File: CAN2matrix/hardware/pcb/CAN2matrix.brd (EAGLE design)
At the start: 100 x 80 mm, 33 parts, among them IC1 MEGA8-P, IC2 MCP2515-E/P, IC3 MCP2515-E/P, U1 MCP2551P, U2 MCP2551P, X1 CAN1, X2 CAN2

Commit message: V1.0 of PCB and adjusted schematics
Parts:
- R4, R5, R6, R7, R8: device resistor:0207/2V -> resistor:0207/10
- R9: device resistor:0207/2V -> resistor:0204/7
- moved R1 53.9 mm to (78.7, 39.4)
- moved PH1 44.4 mm to (29.2, 33.0), turned to 0 degrees
- moved R9 43.1 mm to (30.5, 27.9), turned to 180 degrees
- moved R8 23.2 mm to (44.5, 67.3)
- moved LED5 22.9 mm to (44.5, 76.2)
- moved R4 18.2 mm to (64.8, 67.3)
- moved LED1 17.8 mm to (64.8, 76.2)
- moved R7 13.3 mm to (49.5, 67.3)
- moved LED4 12.7 mm to (49.5, 76.2)
- moved C8 10.2 mm to (40.6, 41.9), turned to 180 degrees
- moved R5 8.52 mm to (59.7, 67.3)
- moved LED2 7.62 mm to (59.7, 76.2)
- moved R6 4.58 mm to (54.6, 67.3)
- moved LED3 2.54 mm to (54.6, 76.2)
- moved C4 1.27 mm to (69.8, 26.7)
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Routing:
- net GND: track 0.00 -> 371.3 mm
- net +5V: track 0.00 -> 213.0 mm
- net N$9: track 0.00 -> 148.2 mm
- net N$1: track 0.00 -> 121.4 mm
- net N$2: track 0.00 -> 116.1 mm
- net N$3: track 0.00 -> 101.3 mm
- net N$16: track 0.00 -> 55.8 mm
- net N$22: track 0.00 -> 50.1 mm
- net N$14: track 0.00 -> 49.7 mm
- net N$7: track 0.00 -> 46.6 mm
- net N$23: track 0.00 -> 43.3 mm
- net N$17: track 0.00 -> 40.9 mm
- net N$19: track 0.00 -> 40.2 mm
- net N$15: track 0.00 -> 36.6 mm
- net N$24: track 0.00 -> 36.4 mm
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- added copper zone on layer 1, net +5V
- added copper zone on layer 16, net GND
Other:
- outline, holes or cut-outs redrawn
- board text added: "Dual CAN"
- board text added: "V1.0"
- board text added: "dev@layer128.net"

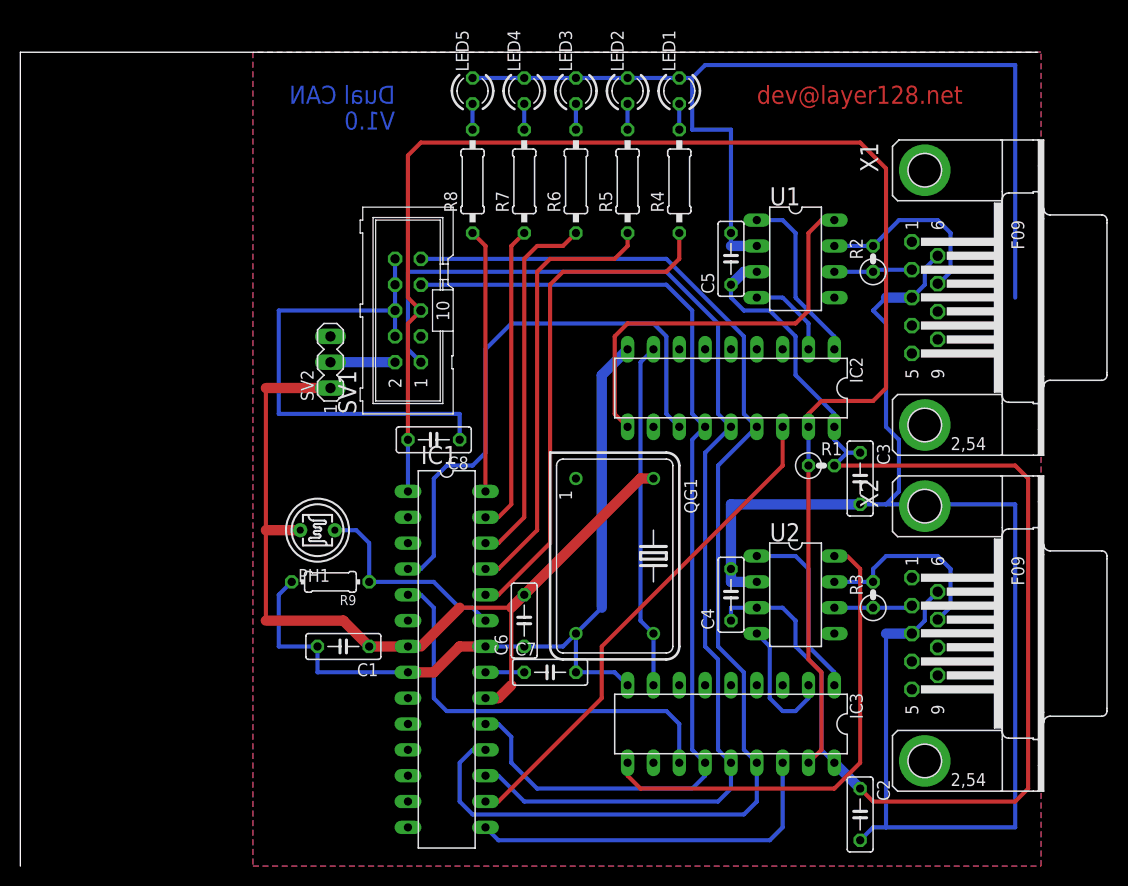
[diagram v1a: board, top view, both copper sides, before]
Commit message: add non-USB power supply to schematics and PCB; export images
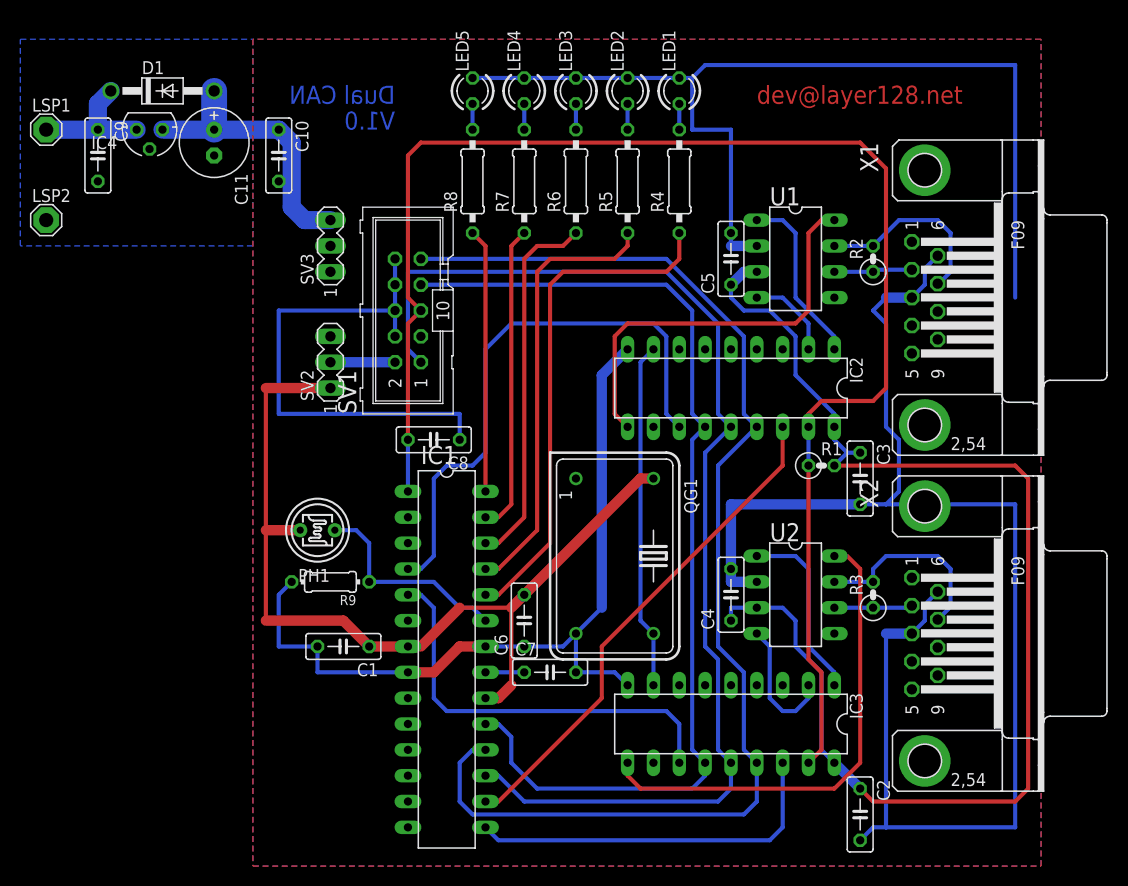
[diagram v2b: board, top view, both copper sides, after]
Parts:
- added C10: 100n, resistor:C050-025X075
- added C11: 1µ, resistor:E2,5-7
- added C9: 330n, resistor:C050-025X075
- added D1: 1N4002, diode:DO41-10
- added IC4: (no value), v-reg:78LXX
- added LSP1: +12V, solpad:SE14
- added LSP2: SE14, solpad:SE14
- added SV3: Ext Pwr, con-lstb:MA03-1
- SV2: value Ext Pwr -> USB Pwr
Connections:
- new net +12V: C9.1, D1.C, IC4.IN, LSP1.MP
- new net N$33: C10.1, C11.+, D1.A, IC4.OUT, SV3.3
- net +5V: now also SV3.2
- net GND: now also C10.2, C11.-, C9.2, IC4.GND, LSP2.MP
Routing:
- net N$33: track 0.00 -> 27.7 mm
- net +12V: track 0.00 -> 13.2 mm
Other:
- board outline removed
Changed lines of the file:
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@@
 <board>
 <plain>
-<wire x1="100" y1="80" x2="0" y2="80" width="0" layer="20"/>
-<wire x1="0" y1="80" x2="0" y2="0" width="0" layer="20"/>
 <text x="36.83" y="74.93" size="1.778" layer="16" rot="MR0">Dual CAN</text>
 <text x="36.83" y="72.39" size="1.778" layer="16" rot="MR0">V1.0</text>
@@
 <attribute name="OC_FARNELL" value="unknown" x="81.28" y="-38.1" size="1.778" layer="27" rot="R270" display="off"/>
 </element>
-<element name="SV2" library="con-lstb" package="MA03-1" value="Ext Pwr" x="30.48" y="49.53" rot="R90">
+<element name="SV2" library="con-lstb" package="MA03-1" value="USB Pwr" x="30.48" y="49.53" rot="R90">
 <attribute name="OC_NEWARK" value="unknown" x="90.17" y="128.27" size="1.778" layer="27" rot="R90" display="off"/>
 <attribute name="MPN" value="" x="90.17" y="128.27" size="1.778" layer="27" rot="R90" display="off"/>
@@
 <element name="R9" library="resistor" package="0204/7" value="39k" x="30.48" y="27.94" rot="R180"/>
 <element name="PH1" library="photo-elements" package="T0-46-A10XX" value="A1050_09" x="29.21" y="33.02"/>
+<element name="IC4" library="v-reg" package="78LXX" value="" x="12.7" y="72.39" rot="R180"/>
+<element name="C9" library="resistor" package="C050-025X075" value="330n" x="7.62" y="69.85" rot="R270"/>
+<element name="C10" library="resistor" package="C050-025X075" value="100n" x="25.4" y="69.85" rot="R270"/>
+<element name="C11" library="resistor" package="E2,5-7" value="1µ" x="19.05" y="71.12" rot="R270"/>
+<element name="D1" library="diode" package="DO41-10" value="1N4002" x="13.97" y="76.2"/>
+<element name="SV3" library="con-lstb" package="MA03-1" value="Ext Pwr" x="30.48" y="60.96" rot="R90">
+<attribute name="OC_NEWARK" value="unknown" x="30.48" y="60.96" size="1.778" layer="27" rot="R90" display="off"/>
+<attribute name="MPN" value="" x="30.48" y="60.96" size="1.778" layer="27" rot="R90" display="off"/>
+<attribute name="MF" value="" x="30.48" y="60.96" size="1.778" layer="27" rot="R90" display="off"/>
+<attribute name="OC_FARNELL" value="unknown" x="30.48" y="60.96" size="1.778" layer="27" rot="R90" display="off"/>
+</element>
+<element name="LSP1" library="solpad" package="SE14" value="+12V" x="2.54" y="72.39"/>
+<element name="LSP2" library="solpad" package="SE14" value="SE14" x="2.54" y="63.5"/>
 </elements>
 <signals>
@@
 <wire x1="71.12" y1="58.42" x2="72.39" y2="58.42" width="1.016" layer="16"/>
 <polygon width="0.4064" layer="1" orphans="yes">
-<vertex x="22.86" y="80.01"/>
+<vertex x="22.86" y="81.28"/>
 <vertex x="22.86" y="0"/>
 <vertex x="100.33" y="0"/>
-<vertex x="100.33" y="80.01"/>
+<vertex x="100.33" y="81.28"/>
 </polygon>
+<contactref element="SV3" pad="2"/>
 </signal>
 <signal name="GND">
@@
 <wire x1="43.18" y1="44.45" x2="25.4" y2="44.45" width="0.4064" layer="16"/>
 <polygon width="0.4064" layer="16" orphans="yes">
-<vertex x="22.86" y="80.01"/>
+<vertex x="22.86" y="81.28"/>
 <vertex x="22.86" y="0"/>
 <vertex x="100.33" y="0"/>
-<vertex x="100.33" y="80.01"/>
+<vertex x="100.33" y="81.28"/>
+</polygon>
+<contactref element="C9" pad="2"/>
+<contactref element="IC4" pad="GND"/>
+<contactref element="C11" pad="-"/>
+<contactref element="C10" pad="2"/>
+<contactref element="LSP2" pad="MP"/>
+<polygon width="0.4064" layer="16" orphans="yes">
+<vertex x="0" y="60.96"/>
+<vertex x="0" y="81.28"/>
+<vertex x="22.86" y="81.28"/>
+<vertex x="22.86" y="60.96"/>
 </polygon>
 </signal>
@@
 <wire x1="30.48" y1="33.02" x2="30.91" y2="33.02" width="0" layer="19" extent="16-16"/>
 </signal>
+<signal name="+12V">
+<contactref element="D1" pad="C"/>
+<contactref element="IC4" pad="IN"/>
+<contactref element="C9" pad="1"/>
+<contactref element="LSP1" pad="MP"/>
+<wire x1="2.54" y1="72.39" x2="7.62" y2="72.39" width="1.778" layer="16"/>
+<wire x1="7.62" y1="72.39" x2="7.62" y2="74.93" width="1.778" layer="16"/>
+<wire x1="7.62" y1="74.93" x2="8.89" y2="76.2" width="1.778" layer="16"/>
+<wire x1="7.62" y1="72.39" x2="11.43" y2="72.39" width="1.778" layer="16"/>
+</signal>
+<signal name="N$33">
+<contactref element="D1" pad="A"/>
+<contactref element="IC4" pad="OUT"/>
+<contactref element="C11" pad="+"/>
+<contactref element="C10" pad="1"/>
+<wire x1="19.05" y1="76.2" x2="19.05" y2="72.39" width="2.54" layer="16"/>
+<wire x1="13.97" y1="72.39" x2="19.05" y2="72.39" width="1.778" layer="16"/>
+<wire x1="19.05" y1="72.39" x2="25.4" y2="72.39" width="1.778" layer="16"/>
+<wire x1="25.4" y1="72.39" x2="26.67" y2="71.12" width="1.778" layer="16"/>
+<contactref element="SV3" pad="3"/>
+<wire x1="26.67" y1="71.12" x2="26.67" y2="64.77" width="1.778" layer="16"/>
+<wire x1="26.67" y1="64.77" x2="27.94" y2="63.5" width="1.778" layer="16"/>
+<wire x1="27.94" y1="63.5" x2="30.48" y2="63.5" width="1.778" layer="16"/>
+</signal>
 </signals>
